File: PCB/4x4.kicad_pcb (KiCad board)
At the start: 2 copper layers, 34 parts

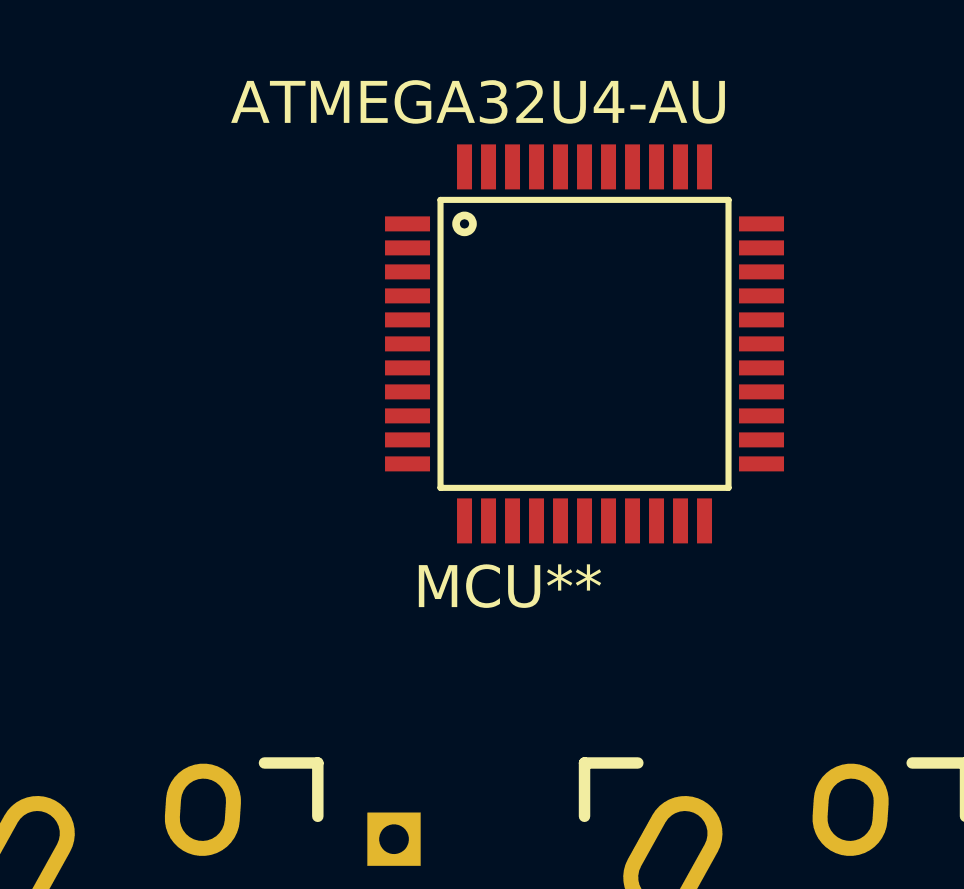
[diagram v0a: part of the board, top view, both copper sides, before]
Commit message: shifted the controller slightly
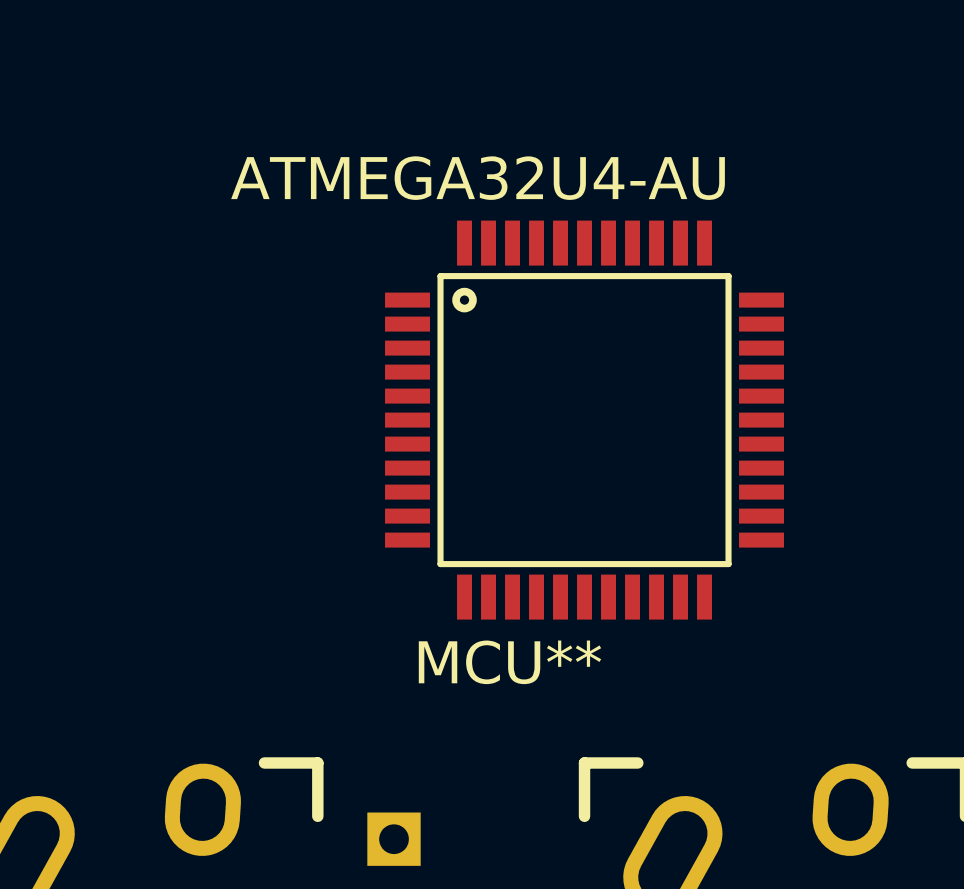
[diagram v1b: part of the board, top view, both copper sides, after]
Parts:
- moved ATMEGA32U4-AU 2.54 mm to (121.9, 40.6)
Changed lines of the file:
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@@
     (links 0)
     (no_connects 0)
-    (area 0 0 0 0)
+    (area 50.8 30.48 139.700001 132.080001)
     (thickness 1.6)
     (drawings 0)
@@
     (pad_to_mask_clearance 0.2)
     (aux_axis_origin 0 0)
-    (visible_elements FFFFFF7F)
+    (visible_elements FFFFF77F)
     (pcbplotparams
       (layerselection 0x00030_80000001)
@@
       (outputformat 1)
       (mirror false)
-      (drillshape 1)
+      (drillshape 0)
       (scaleselection 1)
       (outputdirectory ""))
@@
   )
   (module part_library:ATMEGA32U4-AU (layer F.Cu)
-    (at 121.92 38.1)
+    (at 121.92 40.64)
     (solder_mask_margin 0.1)
     (attr smd)
